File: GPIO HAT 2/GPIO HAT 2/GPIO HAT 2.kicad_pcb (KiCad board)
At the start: 4 copper layers, 85 x 74.7 mm, 109 parts, among them J1 ., J10 ., J11 ., J12 ., J13 ., J14 ., J15 ., J16 ., J17 ., J18 ., J19 ., J2 ., J20 ., J21 LVDS, J22 LVDS, J23 02x02, J24 USB_C_Receptacle_PowerOnly_6P, J25 SMD PAD, J3 ., J4 ., J5 ., J6 ., J7 ., J8 ., J9 ., U1 TXB0108DQSR, U10 TXB0108DQSR, U12 SY8088IAAC, U13 SY8088IAAC, U14 TPS2117, U2 TXB0108DQSR, U3 TXB0108DQSR, U4 TXB0108DQSR, U5 TXB0108DQSR, U6 TXB0108DQSR, U7 TXB0108DQSR, U8 TXB0108DQSR, U9 TXB0108DQSR

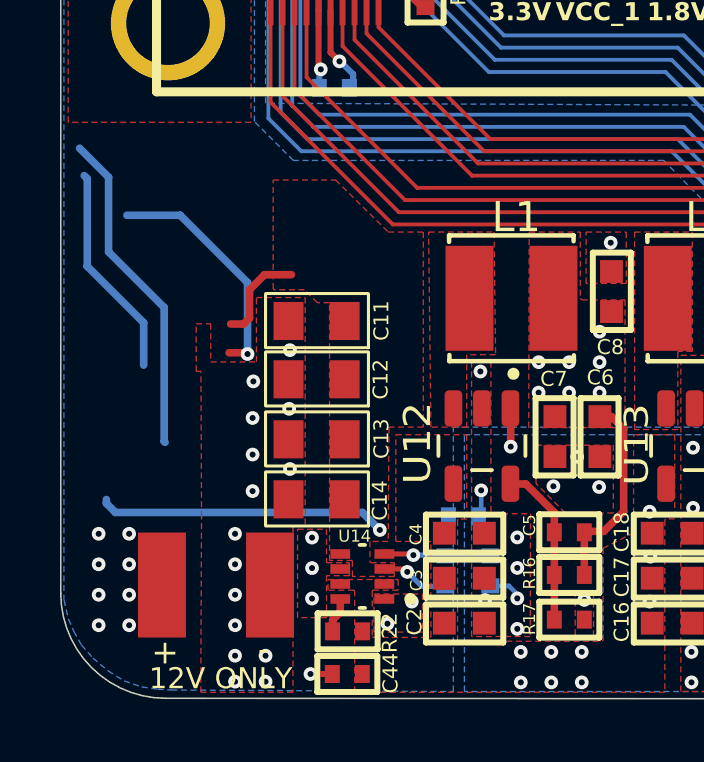
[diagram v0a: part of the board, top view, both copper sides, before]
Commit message: 12V Jack removed and 5V USB added
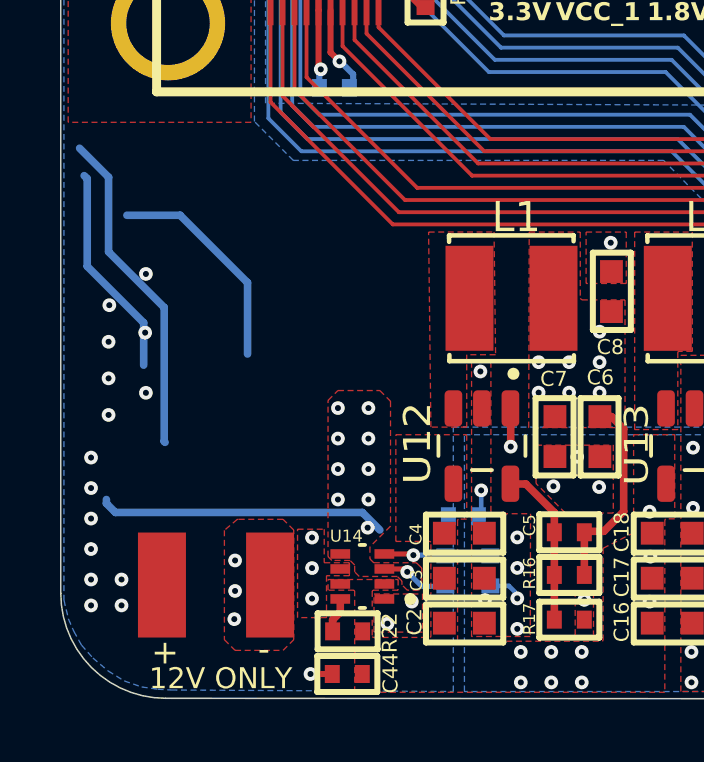
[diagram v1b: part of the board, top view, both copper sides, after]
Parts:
- removed C11, C12, C13, C14: 22uF, VAAMAN2:0805_Cap
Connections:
- J25 pad 1: 5V_1 -> GND
- J25 pad 2: GND -> 5V_1
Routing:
- net (no net): track 26.1 -> 18.3 mm, vias 1 -> 0
- net GND: track 129.0 -> 136.1 mm
- net 5V_1: track 15.1 -> 11.9 mm, vias 10 -> 13
- added copper zone on In2.Cu, net 5V_1
- removed copper zone on In2.Cu, net 5V

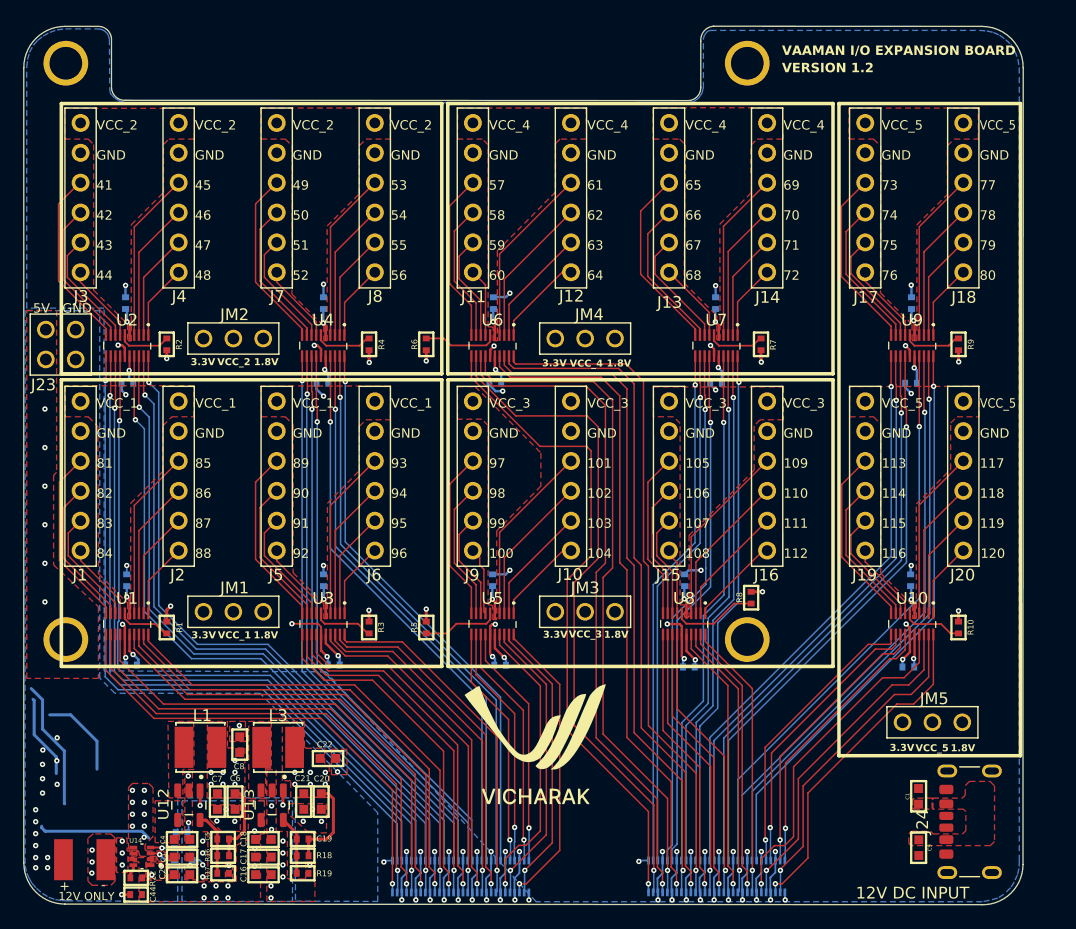
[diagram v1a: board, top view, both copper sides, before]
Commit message: Ground plane added to top layer
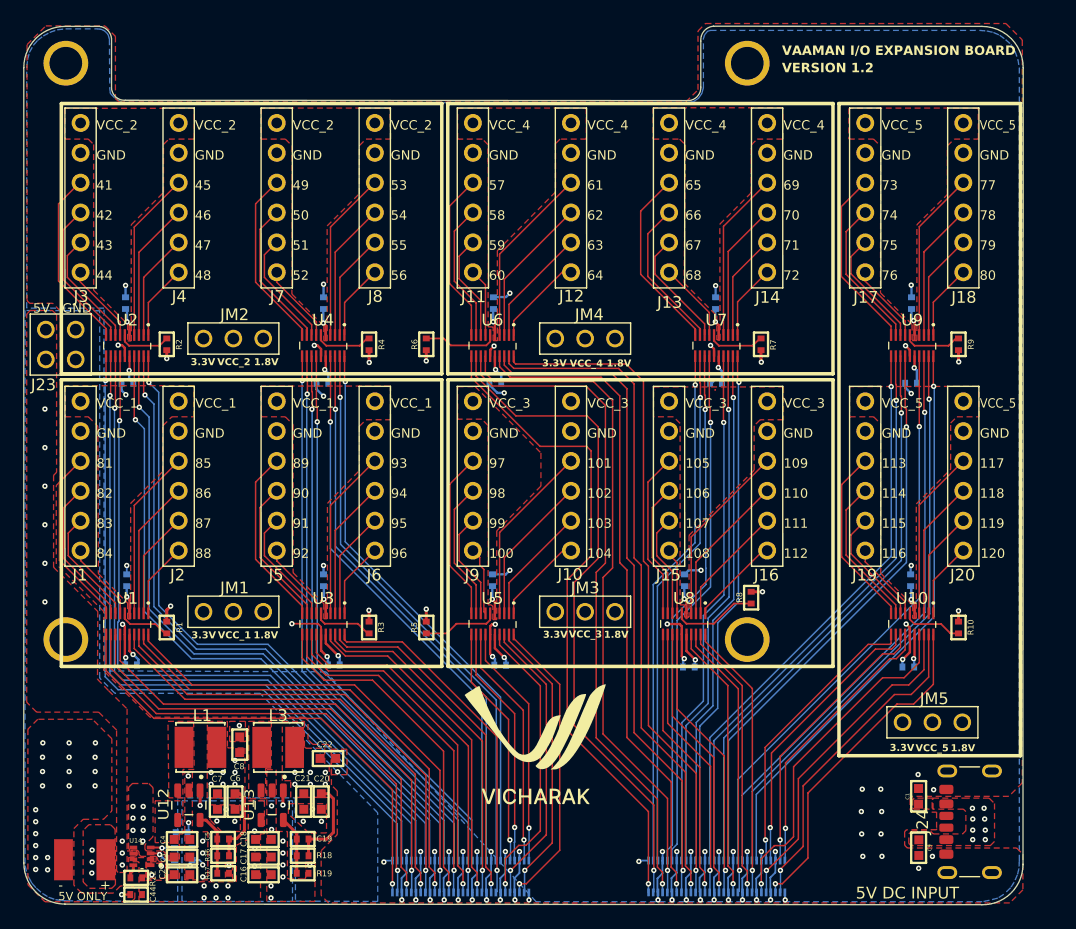
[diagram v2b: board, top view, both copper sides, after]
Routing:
- net (no net): track 18.3 -> 0.00 mm
- net 5V_1: track 11.9 -> 2.28 mm, vias 13 -> 19
- net GND: track 136.1 -> 128.9 mm, vias 113 -> 129
- removed copper zone on In1.Cu, net GND
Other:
- board text added: "5V DC INPUT"
- board text added: "5V ONLY"
- board text removed: "12V DC INPUT"
- board text removed: "12V ONLY"

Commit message: Update
Gerber Generated
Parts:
- moved G*** 4.95 mm to (194.4, 123.0)
- renumbered C2 to C1, C44 to C10, C43 to C11, C16 to C12, C17 to C13, C18 to C14, C19 to C15, C20 to C16, C21 to C17, C22 to C18, C24 to C19, C3 to C2, C26 to C20, C28 to C21, C34 to C22, C36 to C23, C38 to C24, C23 to C25, C25 to C26, C33 to C28, C35 to C29, C4 to C3, C37 to C30, C30 to C31, C40 to C33, C42 to C34, C29 to C35, C31 to C36, C39 to C37, C41 to C38, C5 to C4, C6 to C5, C7 to C6, C8 to C7, C1 to C8, J24 to J1, J15 to J10, J2 to J11, J4 to J12, J6 to J13, J12 to J14, J14 to J15, J7 to J17, J9 to J18, J17 to J19, J23 to J2, J19 to J20, J8 to J21, J10 to J22, J18 to J23, J20 to J24, J22 to J3, J21 to J4, J1 to J5, J3 to J6, J5 to J7, J11 to J8, J13 to J9, JM2 to JM1, JM4 to JM2, JM1 to JM3, JM3 to JM4, L3 to L2, R16 to R1, R3 to R10, R6 to R11, R7 to R12, R8 to R13, R4 to R14, R5 to R15, R9 to R16, R10 to R17, R17 to R2, R20 to R3, R22 to R4, R21 to R5, R18 to R6, R19 to R7, R1 to R8, R2 to R9, U12 to U1, U4 to U10, U5 to U11, U9 to U12, U10 to U13, U14 to U2, U13 to U3, U1 to U4, U2 to U5, U3 to U6, U6 to U7, U7 to U8, U8 to U9
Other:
- board text added: "Designed in Gujarat,India."
- board text added: "R0.2"
- board text added: "V1.0"
- board text removed: "VERSION 1.2"

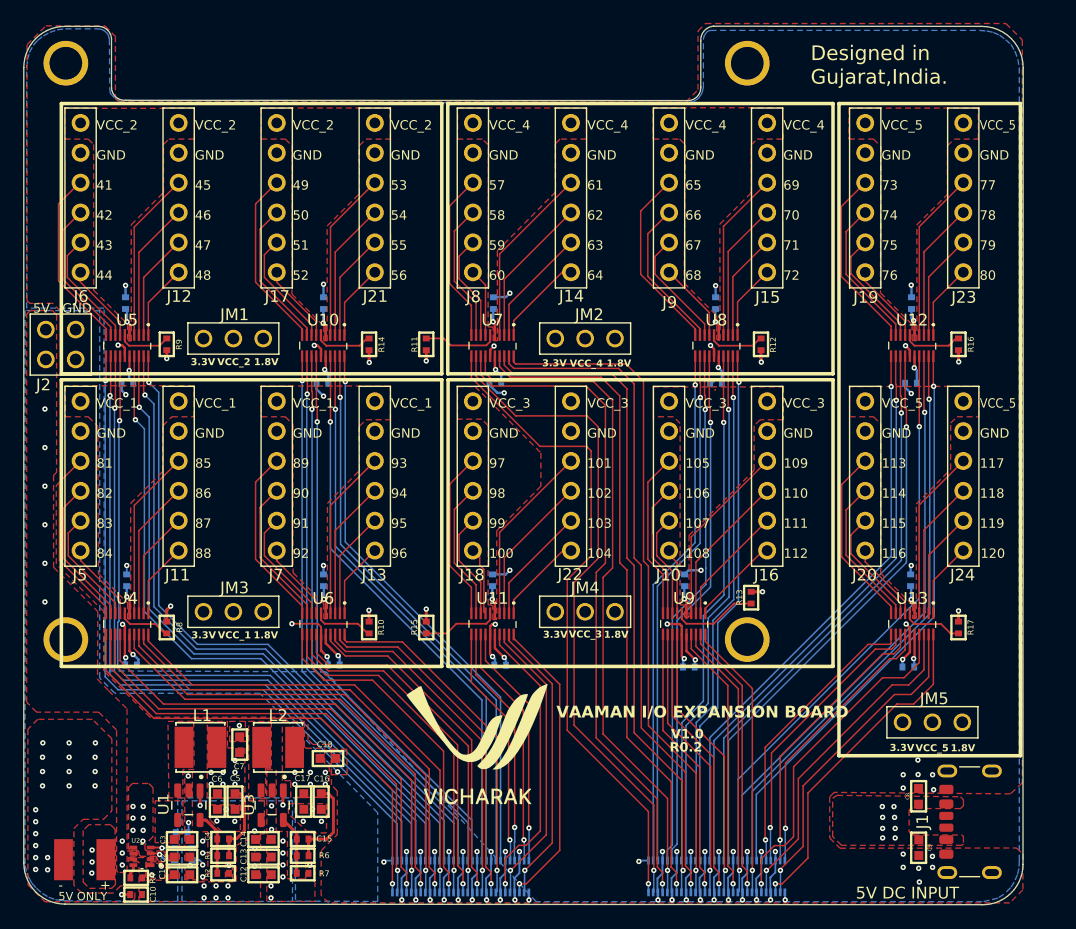
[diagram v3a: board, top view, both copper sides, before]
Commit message: GPIO number change, CC1 & CC2 tied to GND
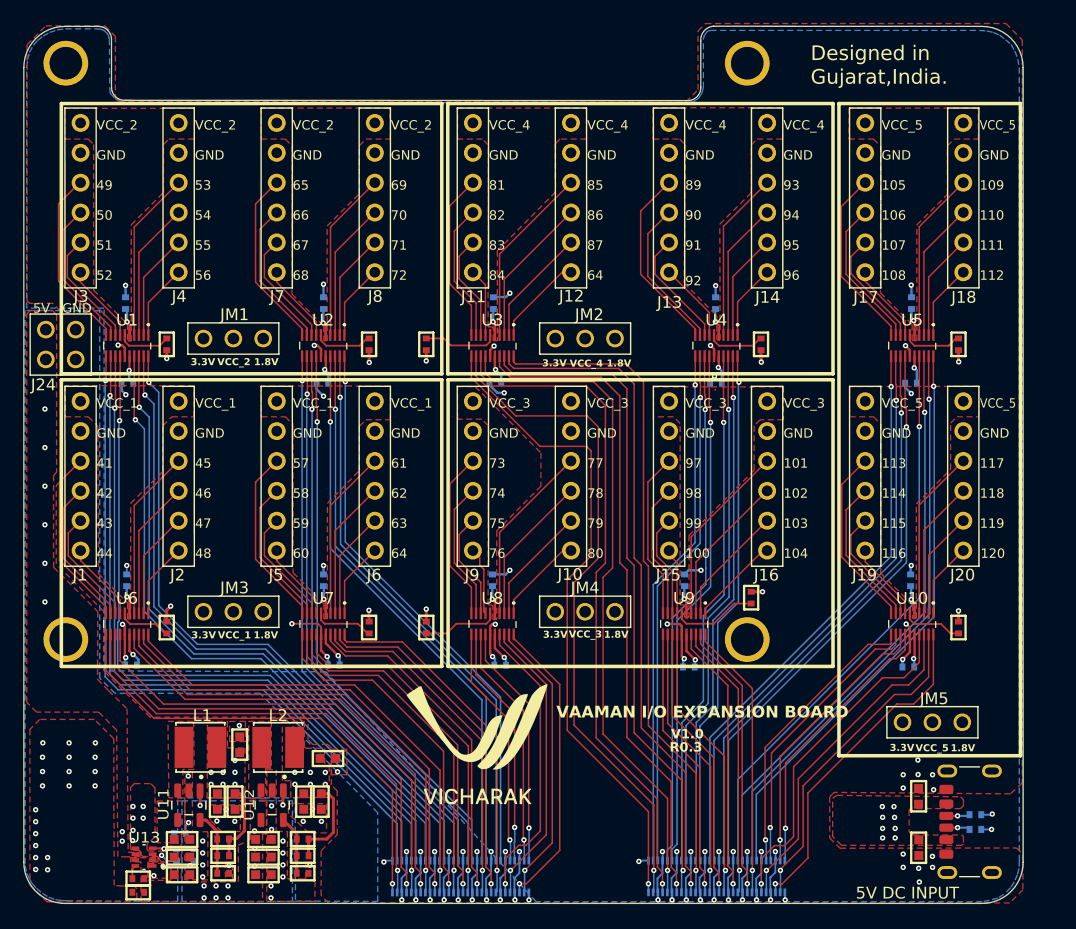
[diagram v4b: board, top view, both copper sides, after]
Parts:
- removed J25: SMD PAD, VAAMAN2:12V SMD PAD
- removed the U2 at (165.9, 132.6)
- added R18: 5.1K, VAAMAN2:0402_Res, B.Cu at (236.7, 129.1)
- added R19: 5.1K, VAAMAN2:0402_Res, B.Cu at (236.7, 130.3)
- added U13: TPS2117, VAAMAN2:TPS2117, F.Cu at (166.0, 132.7)
- moved C10 0.27 mm to (165.6, 135.7)
- moved R3 0.18 mm to (168.8, 132.5)
- moved R4 0.18 mm to (165.5, 134.6)
- moved R5 0.18 mm to (170.3, 132.5)
- moved C11 0.17 mm to (169.1, 130.7)
- renumbered J5 to J1, J22 to J10, J8 to J11, J14 to J12, J9 to J13, J15 to J14, J10 to J15, J19 to J17, J23 to J18, J20 to J19, J11 to J2, J24 to J20, J4 to J21, J3 to J22, J1 to J23, J2 to J24, J6 to J3, J12 to J4, J7 to J5, J13 to J6, J17 to J7, J21 to J8, J18 to J9, U5 to U1, U13 to U10, U1 to U11, U3 to U12, U10 to U2, U7 to U3, U8 to U4, U12 to U5, U4 to U6, U6 to U7, U11 to U8
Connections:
- J23 pad A5: unconnected-(J1-CC1-PadA5) -> Net-(J23-CC1)
- J23 pad B5: unconnected-(J1-CC2-PadB5) -> Net-(J23-CC2)
- J23 pad B9: 5V_1 -> unconnected-(J23-VBUS-PadB9)
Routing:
- net Net-(J23-CC1): track 0.00 -> 2.03 mm, vias 0 -> 1
- net Net-(J23-CC2): track 0.00 -> 2.01 mm, vias 0 -> 1
- net 5V_1: track 2.28 -> 1.44 mm, vias 19 -> 15
- net GND: track 128.9 -> 129.4 mm, vias 129 -> 131
- net VCC5V: vias 9 -> 8
- added copper zone on In1.Cu, net GND
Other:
- board size 85 x 74.7 mm -> 85 x 74.6 mm
- board text added: "R0.3"
- board text removed: "+"
- board text removed: "-"
- board text removed: "5V ONLY"
- board text removed: "88"
- board text removed: "R0.2"
